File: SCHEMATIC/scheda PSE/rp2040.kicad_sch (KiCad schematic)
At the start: 26 parts, among them J1 Conn_01x03, SW1 RESET_SW, SW2 PROG_SW, U1 RP2040, U2 W25Q16JVUSSQ, U3 AT24C256, Y1 12MHz

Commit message: cambiati i pulsanti in smd
se servono gli altri pulsanti usare la versione precedente
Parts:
- SW1, SW2: footprint Button_Switch_THT:SW_PUSH_6mm_H5mm -> Button_Switch_SMD:SW_SPST_EVQP0
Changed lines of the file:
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@@
       (effects (font (size 1.27 1.27)) (justify right))
     )
-    (property "Footprint" "Button_Switch_THT:SW_PUSH_6mm_H5mm" (id 2) (at 24.765 128.905 0)
+    (property "Footprint" "Button_Switch_SMD:SW_SPST_EVQP0" (id 2) (at 24.765 128.905 0)
       (effects (font (size 1.27 1.27)) hide)
     )
@@
       (effects (font (size 1.27 1.27)) (justify left))
     )
-    (property "Footprint" "Button_Switch_THT:SW_PUSH_6mm_H5mm" (id 2) (at 274.955 149.86 0)
+    (property "Footprint" "Button_Switch_SMD:SW_SPST_EVQP0" (id 2) (at 274.955 149.86 0)
       (effects (font (size 1.27 1.27)) hide)
     )

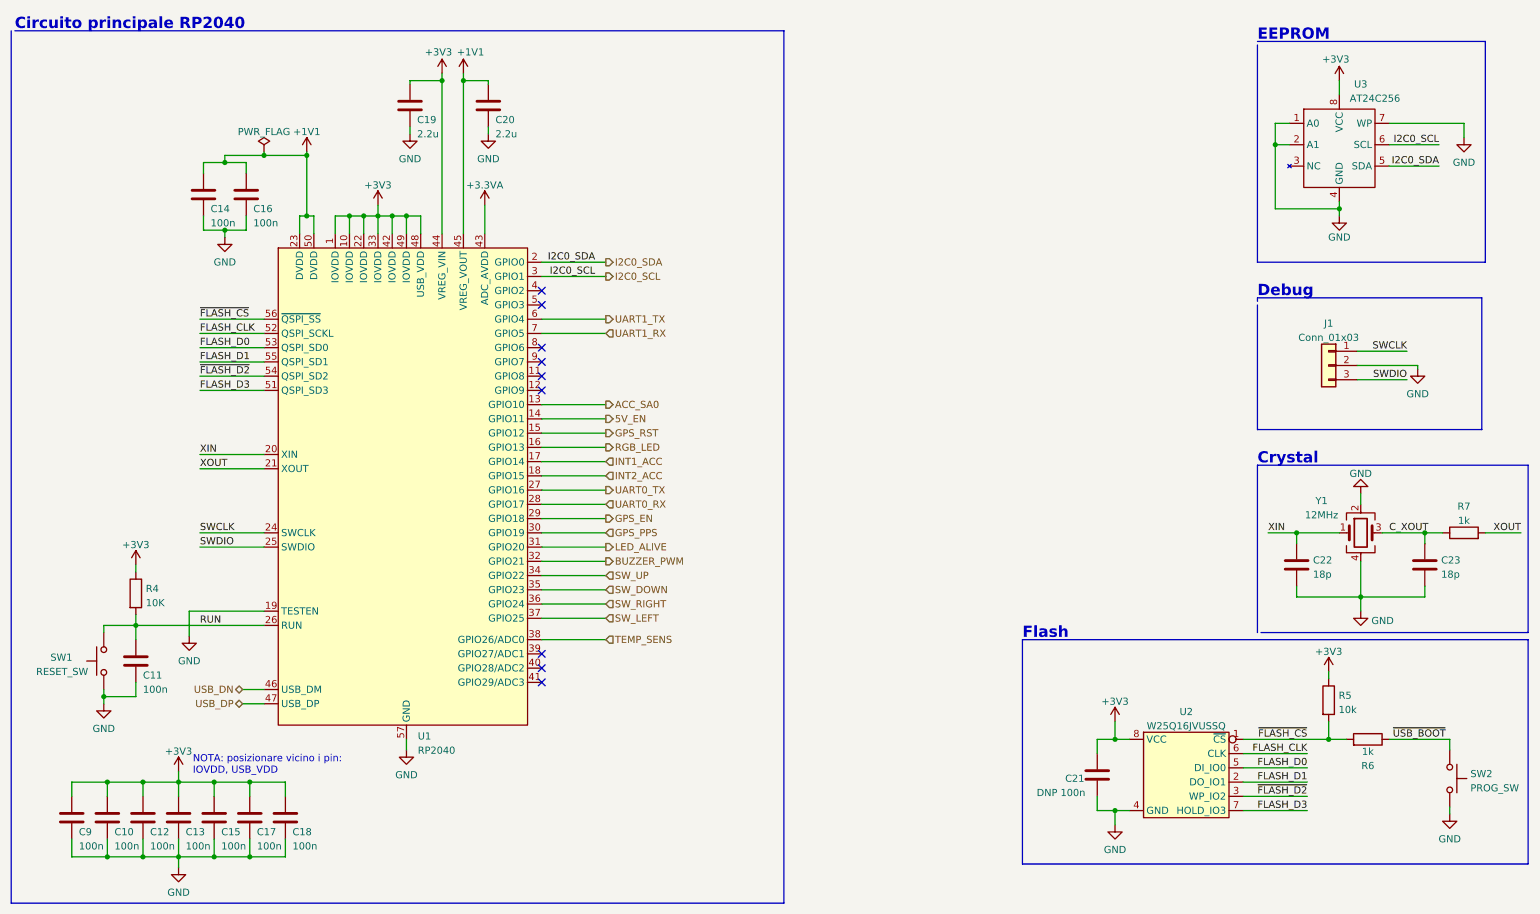
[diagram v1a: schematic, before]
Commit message: Aggiunte tutte le cose richieste dal prof
Aggiunte tutte le cose richieste dal prof:
wifi
servo
uscita led
MANCA DA METERE IL SOLDER MASK SUI PAD NON USATI DEL GPS
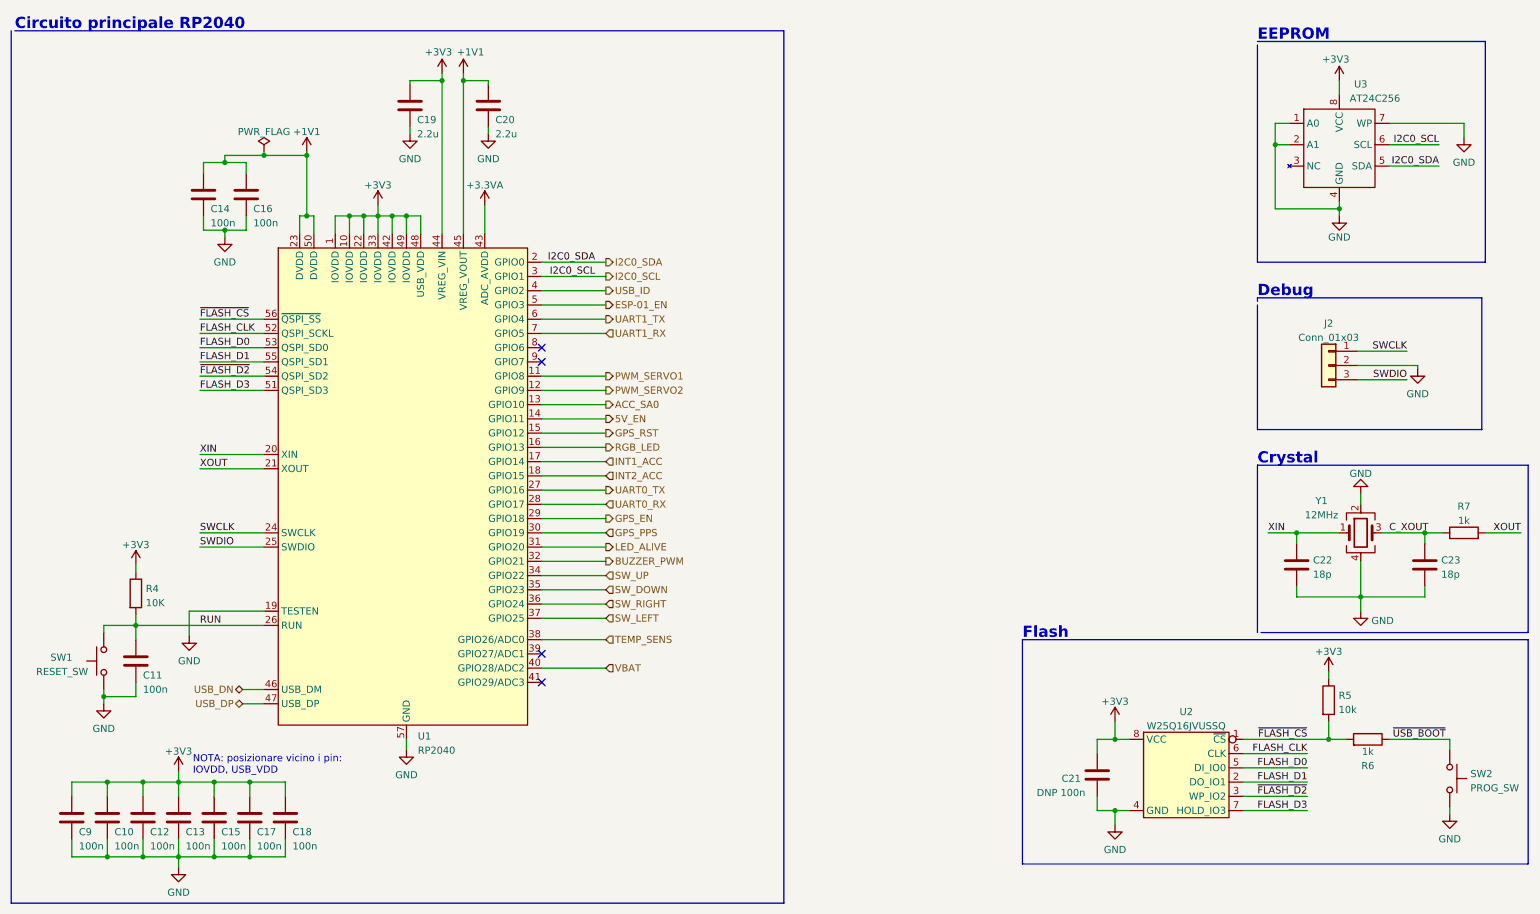
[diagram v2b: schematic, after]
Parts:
- renumbered J1 to J2
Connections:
- net PWM_SERVO1: now reaches U1.11 (GPIO8)
- net PWM_SERVO2: now reaches U1.12 (GPIO9)
- net USB_ID: now reaches U1.4 (GPIO2)
- net VBAT: now reaches U1.40 (GPIO28/ADC2)
- net ESP-01_EN: now reaches U1.5 (GPIO3)
- no-connect marks 9 -> 4

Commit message: Sistemate un po'di cose
aggiuno fori display e terzo servo e sistemate le serigrafie
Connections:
- net PWM_SERVO3: now reaches U1.9 (GPIO7)
- no-connect marks 4 -> 3
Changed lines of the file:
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@@
   (no_connect (at 107.95 132.715))
   (no_connect (at 107.95 73.025))
-  (no_connect (at 107.95 75.565))
   (polyline (pts (xy 193.675 165.1) (xy 283.845 165.1))
     (stroke (width 0) (type default) (color 0 0 0 0))
@@
   )
   (wire (pts (xy 107.95 62.865) (xy 119.38 62.865))
+    (stroke (width 0) (type default) (color 0 0 0 0))
+  )
+  (wire (pts (xy 107.95 75.565) (xy 119.38 75.565))
     (stroke (width 0) (type default) (color 0 0 0 0))
   )
@@
     (effects (font (size 1.27 1.27)) (justify left))
   )
+  (hierarchical_label "PWM_SERVO3" (shape output) (at 119.38 75.565 0)
+    (effects (font (size 1.27 1.27)) (justify left))
+  )

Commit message: Aggiunto mosfet uscita corrente usb
Ultima modifica prima della revisone generale.
aggiunto un mosfet P per l'attivazione dell'uscita della tensione alla usb in caso di master
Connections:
- net OUTPUT_USB_EN: now reaches U1.39 (GPIO27/ADC1)
- no-connect marks 3 -> 2
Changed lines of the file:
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@@
   (junction (at 55.88 163.83) (diameter 0) (color 0 0 0 0)
   )
-  (no_connect (at 107.95 127.635))
   (no_connect (at 107.95 132.715))
   (no_connect (at 107.95 73.025))
@@
     (stroke (width 0) (type default) (color 0 0 0 0))
   )
+  (wire (pts (xy 107.95 127.635) (xy 119.38 127.635))
+    (stroke (width 0) (type default) (color 0 0 0 0))
+  )
   (polyline (pts (xy 235.585 64.135) (xy 235.585 64.77))
     (stroke (width 0) (type default) (color 0 0 0 0))
@@
     (effects (font (size 1.27 1.27)) (justify left))
   )
+  (hierarchical_label "OUTPUT_USB_EN" (shape output) (at 119.38 127.635 0)
+    (effects (font (size 1.27 1.27)) (justify left))
+  )

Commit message: Versione definitiva inviata ai prof
Sistemato tutto e inviato il tutto ai prof
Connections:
- net ACC_SA0: no longer names the net of U1.13 (GPIO10)
- no-connect marks 2 -> 3
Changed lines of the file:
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@@
   (no_connect (at 107.95 132.715))
   (no_connect (at 107.95 73.025))
+  (no_connect (at 107.95 83.185))
   (polyline (pts (xy 193.675 165.1) (xy 283.845 165.1))
     (stroke (width 0) (type default) (color 0 0 0 0))
@@
   )
   (wire (pts (xy 107.95 57.785) (xy 119.38 57.785))
-    (stroke (width 0) (type default) (color 0 0 0 0))
-  )
-  (wire (pts (xy 107.95 83.185) (xy 119.38 83.185))
     (stroke (width 0) (type default) (color 0 0 0 0))
   )
@@
     (effects (font (size 1.27 1.27)) (justify left))
   )
-  (hierarchical_label "ACC_SA0" (shape output) (at 119.38 83.185 0)
-    (effects (font (size 1.27 1.27)) (justify left))
-  )
